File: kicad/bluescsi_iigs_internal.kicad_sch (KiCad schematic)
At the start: 27 parts, among them J1 Conn_02x13_Odd_Even, J2 Conn_02x13_Odd_Even, J3 105162-0001, J4 Conn_01x02_Male, J5 Conn_01x02_Male, J6 DB25_Male, M1 Screw_Terminal_01x01, M2 Screw_Terminal_01x01, SW1 SW_SPDT, U1 YAAJ_BluePill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

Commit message: added part numbers
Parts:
- C1, C2: value 4.7uF, 6.3v -> (none); footprint Capacitor_Tantalum_SMD:CP_EIA-3528-21_Kemet-B_Pad1.50x2.35mm_HandSolder -> (none); DESCRIPTION (none) -> 2.2uF 6.3V CASE-B_3528 Tantalum Capacitor; LCSC part number (none) -> C19276; MANUFACTURER_NAME (none) -> Kyocera AVX; MANUFACTURER_PART_NUMBER (none) -> TAJB225K035RNJ
- C3: value 4.7uF, 6.3v -> (none); footprint Capacitor_Tantalum_SMD:CP_EIA-3528-21_Kemet-B_Pad1.50x2.35mm_HandSolder -> (none); DESCRIPTION (none) -> 4.7uF 6.3V CASE-B_3528 Tantalum Capacitor; LCSC part number (none) -> C7204; MANUFACTURER_NAME (none) -> Kyocera AVX; MANUFACTURER_PART_NUMBER (none) -> TAJB475K016RNJ
- C4: value 1uF -> (none); footprint Capacitor_Tantalum_SMD:CP_EIA-3528-21_Kemet-B_Pad1.50x2.35mm_HandSolder -> (none); DESCRIPTION (none) -> 1uF 6.3V CASE-B_3528 Tantalum Capacitor; LCSC part number (none) -> C7192; MANUFACTURER_NAME (none) -> Kyocera AVX; MANUFACTURER_PART_NUMBER (none) -> TAJB105K035RNJ
- C5: value 0.1uF -> (none); footprint Capacitor_Tantalum_SMD:CP_EIA-3528-21_Kemet-B_Pad1.50x2.35mm_HandSolder -> (none); DESCRIPTION (none) -> 100nF 35V CASE-A_3216 Tantalum Capacitor; LCSC part number (none) -> C122257; MANUFACTURER_NAME (none) -> KEMET; MANUFACTURER_PART_NUMBER (none) -> T491A104K035AT
- D1: value LED -> (none); footprint LED_SMD:LED_0805_2012Metric_Pad1.15x1.40mm_HandSolder -> (none); DESCRIPTION (none) -> 0805 Blue LED; LCSC part number (none) -> C497961; MANUFACTURER_NAME (none) -> HONGLITRONIC(Hongli Zhihui (HONGLITRONIC)); MANUFACTURER_PART_NUMBER (none) -> HL-PSC-2012H203BC
- D2: value LED -> (none); footprint LED_SMD:LED_0805_2012Metric_Pad1.15x1.40mm_HandSolder -> (none); DESCRIPTION (none) -> 0805 Red LED; LCSC part number (none) -> C84256; MANUFACTURER_NAME (none) -> Foshan NationStar Optoelectronics; MANUFACTURER_PART_NUMBER (none) -> NCD0805R1
- D3: value Zener 5.6v -> (none); footprint Diode_SMD:D_SOD-123 -> (none); DESCRIPTION (none) -> 5.6V SOD-123 Zener Diode; LCSC part number (none) -> C268592; MANUFACTURER_NAME (none) -> PANJIT International; MANUFACTURER_PART_NUMBER (none) -> MMSZ5232A_R1_00001
- F1: value Fuse -> (none); footprint Fuse:Fuse_1210_3225Metric -> (none); DESCRIPTION (none) -> SMD 1206 Fuse 800mA 63V; LCSC part number (none) -> C163134; MANUFACTURER_NAME (none) -> TA-I Tech; MANUFACTURER_PART_NUMBER (none) -> CFS12V6TR80
- J1, J2: value Conn_02x13_Odd_Even -> (none); footprint Connector_PinHeader_2.54mm:PinHeader_2x13_P2.54mm_Vertical -> (none)
- J3: value 105162-0001 -> (none); footprint Molex 105162-0001:105162-0001 -> (none); LCSC part number (none) -> C724031
- J4, J5: value Conn_01x02_Male -> (none); footprint Connector_PinHeader_2.54mm:PinHeader_1x02_P2.54mm_Vertical -> (none)
- J6: value DB25_Male -> (none); footprint Connector_Dsub:DSUB-25_Male_EdgeMount_P2.77mm -> (none)
- JP1, JP2: value Jumper_3_Open -> (none); footprint Jumper:SolderJumper-3_P1.3mm_Open_Pad1.0x1.5mm_NumberLabels -> (none)
- M1, M2: value Screw_Terminal_01x01 -> (none); footprint my library:keystone-7774 -> (none)
- R1: value 110 -> (none); footprint Resistor_SMD:R_0805_2012Metric_Pad1.20x1.40mm_HandSolder -> (none); DESCRIPTION (none) -> 100Ω 0805 Chip Resistor - Surface Mount; LCSC part number (none) -> C17408; MANUFACTURER_NAME (none) -> UNI-ROYAL(Uniroyal Elec); MANUFACTURER_PART_NUMBER (none) -> 0805W8F1000T5E
- R2: value 1K -> (none); footprint Resistor_SMD:R_0805_2012Metric_Pad1.20x1.40mm_HandSolder -> (none); DESCRIPTION (none) -> 1KΩ 0805 Chip Resistor - Surface Mount; LCSC part number (none) -> C17513; MANUFACTURER_NAME (none) -> UNI-ROYAL(Uniroyal Elec); MANUFACTURER_PART_NUMBER (none) -> 0805W8F1001T5E
- SW1: value SW_SPDT -> (none); footprint Button_Switch_SMD:SW_SPDT_PCM12 -> (none); DESCRIPTION (none) -> SMD Slide Switch; LCSC part number (none) -> C221841; MANUFACTURER_NAME (none) -> C&K; MANUFACTURER_PART_NUMBER (none) -> PCM12SMTR
- U1: value YAAJ_BluePill -> (none); footprint my library:YAAJ_BluePill_2 -> (none)
- U2, U3: value UC560x, UCC56xx -> (none); footprint my library:SOIC127P600X175-16N -> (none)
- U4: value UCC3916 -> (none); footprint Package_SO:SOIC-8_3.9x4.9mm_P1.27mm -> (none)
- U5: value NL17SZ07DFT2G -> (none); footprint Package_TO_SOT_SMD:SOT-353_SC-70-5_Handsoldering -> (none); DESCRIPTION (none) -> Open Drain 24mA Buffers，Unidirectional Voltage Level Transl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; LCSC part number (none) -> C113255; MANUFACTURER_NAME (none) -> onsemi; MANUFACTURER_PART_NUMBER (none) -> NL17SZ07DFT2G

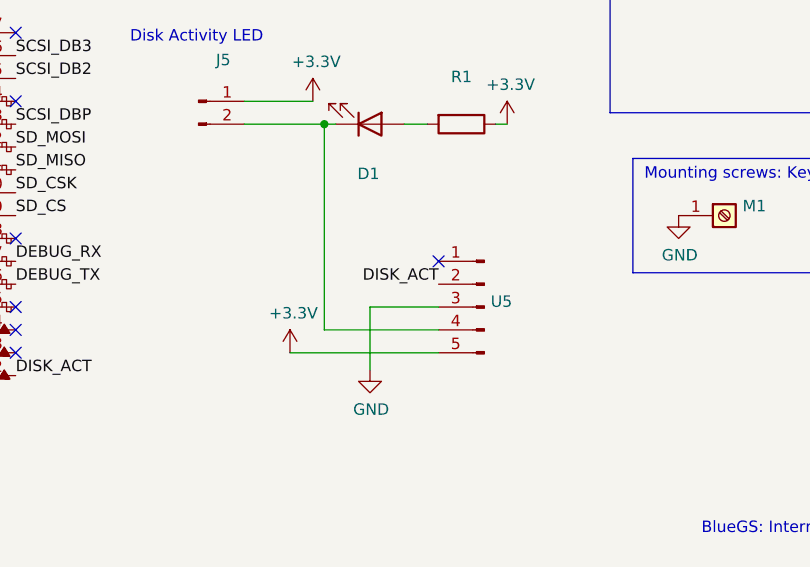
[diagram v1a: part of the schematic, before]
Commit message: Added compatibility for 74LVC1G125SE in place of NL17SZ07DFT2G
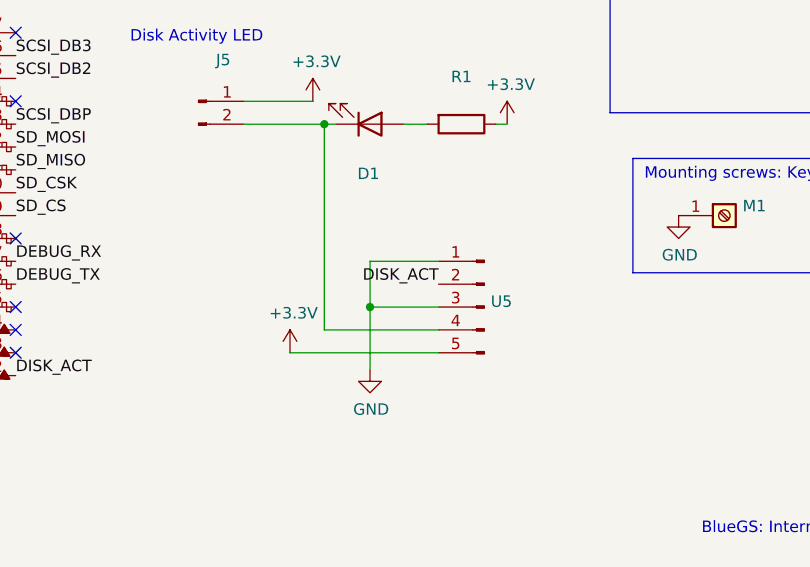
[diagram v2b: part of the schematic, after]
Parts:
- C1, C2: LCSC part number C19276 -> C444753; MANUFACTURER_PART_NUMBER TAJB225K035RNJ -> TAJB225M020RNJ
- C3: LCSC part number C7204 -> C918865; MANUFACTURER_NAME Kyocera AVX -> KEMET; MANUFACTURER_PART_NUMBER TAJB475K016RNJ -> T494B475K016AT
- C4: LCSC part number C7192 -> C452761; MANUFACTURER_NAME Kyocera AVX -> KEMET; MANUFACTURER_PART_NUMBER TAJB105K035RNJ -> T491B105K025AT
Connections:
- net GND: now also U5.1 (Pin_1)
- no-connect marks 14 -> 13
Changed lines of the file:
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@@
   (junction (at 167.64 114.3) (diameter 0) (color 0 0 0 0)
+  )
+  (junction (at 149.86 165.1) (diameter 0) (color 0 0 0 0)
   )
   (junction (at 167.64 116.84) (diameter 0) (color 0 0 0 0)
@@
   (no_connect (at 110.49 134.62))
   (no_connect (at 69.85 152.4))
-  (no_connect (at 157.48 160.02))
   (no_connect (at 167.64 106.68))
   (no_connect (at 110.49 167.64))
@@
     (stroke (width 0) (type default) (color 0 0 0 0))
   )
+  (wire (pts (xy 149.86 160.02) (xy 149.86 165.1))
+    (stroke (width 0) (type default) (color 0 0 0 0))
+  )
   (wire (pts (xy 144.78 144.78) (xy 146.05 144.78))
     (stroke (width 0) (type default) (color 0 0 0 0))
@@
   )
   (wire (pts (xy 214.63 116.205) (xy 216.535 116.205))
+    (stroke (width 0) (type default) (color 0 0 0 0))
+  )
+  (wire (pts (xy 157.48 160.02) (xy 149.86 160.02))
     (stroke (width 0) (type default) (color 0 0 0 0))
   )
@@
       (effects (font (size 1.27 1.27)) hide)
     )
-    (property "MANUFACTURER_NAME" "Kyocera AVX" (id 4) (at 261.62 38.1 0)
-      (effects (font (size 1.27 1.27)) hide)
-    )
-    (property "MANUFACTURER_PART_NUMBER" "TAJB475K016RNJ" (id 5) (at 261.62 38.1 0)
+    (property "MANUFACTURER_NAME" "KEMET" (id 4) (at 261.62 38.1 0)
+      (effects (font (size 1.27 1.27)) hide)
+    )
+    (property "MANUFACTURER_PART_NUMBER" "T494B475K016AT" (id 5) (at 261.62 38.1 0)
       (effects (font (size 1.27 1.27)) hide)
     )
@@
       (effects (font (size 1.27 1.27)) hide)
     )
-    (property "LCSC part number" "C7204" (id 7) (at 261.62 38.1 0)
+    (property "LCSC part number" "C918865" (id 7) (at 261.62 38.1 0)
       (effects (font (size 1.27 1.27)) hide)
     )
@@
       (effects (font (size 1.27 1.27)) hide)
     )
-    (property "MANUFACTURER_PART_NUMBER" "TAJB225K035RNJ" (id 5) (at 130.81 39.37 0)
+    (property "MANUFACTURER_PART_NUMBER" "TAJB225M020RNJ" (id 5) (at 130.81 39.37 0)
       (effects (font (size 1.27 1.27)) hide)
     )
@@
       (effects (font (size 1.27 1.27)) hide)
     )
-    (property "LCSC part number" "C19276" (id 7) (at 130.81 39.37 0)
+    (property "LCSC part number" "C444753" (id 7) (at 130.81 39.37 0)
       (effects (font (size 1.27 1.27)) hide)
     )
@@
       (effects (font (size 1.27 1.27)) hide)
     )
-    (property "MANUFACTURER_PART_NUMBER" "TAJB225K035RNJ" (id 5) (at 130.81 67.31 0)
+    (property "MANUFACTURER_PART_NUMBER" "TAJB225M020RNJ" (id 5) (at 130.81 67.31 0)
       (effects (font (size 1.27 1.27)) hide)
     )
@@
       (effects (font (size 1.27 1.27)) hide)
     )
-    (property "LCSC part number" "C19276" (id 7) (at 130.81 67.31 0)
+    (property "LCSC part number" "C444753" (id 7) (at 130.81 67.31 0)
       (effects (font (size 1.27 1.27)) hide)
     )
@@
       (effects (font (size 1.27 1.27)) hide)
     )
-    (property "MANUFACTURER_NAME" "Kyocera AVX" (id 4) (at 232.41 120.015 0)
-      (effects (font (size 1.27 1.27)) hide)
-    )
-    (property "MANUFACTURER_PART_NUMBER" "TAJB105K035RNJ" (id 5) (at 232.41 120.015 0)
+    (property "MANUFACTURER_NAME" "KEMET" (id 4) (at 232.41 120.015 0)
+      (effects (font (size 1.27 1.27)) hide)
+    )
+    (property "MANUFACTURER_PART_NUMBER" "T491B105K025AT" (id 5) (at 232.41 120.015 0)
       (effects (font (size 1.27 1.27)) hide)
     )
@@
       (effects (font (size 1.27 1.27)) hide)
     )
-    (property "LCSC part number" "C7192" (id 7) (at 232.41 120.015 0)
-      (effects (font (size 1.27 1.27)) hide)
-    )
+    (property "LCSC part number" "C452761" (id 7) (at 232.41 120.015 0)
+      (effects (font (size 1.27 1.27)) hide)
+    )

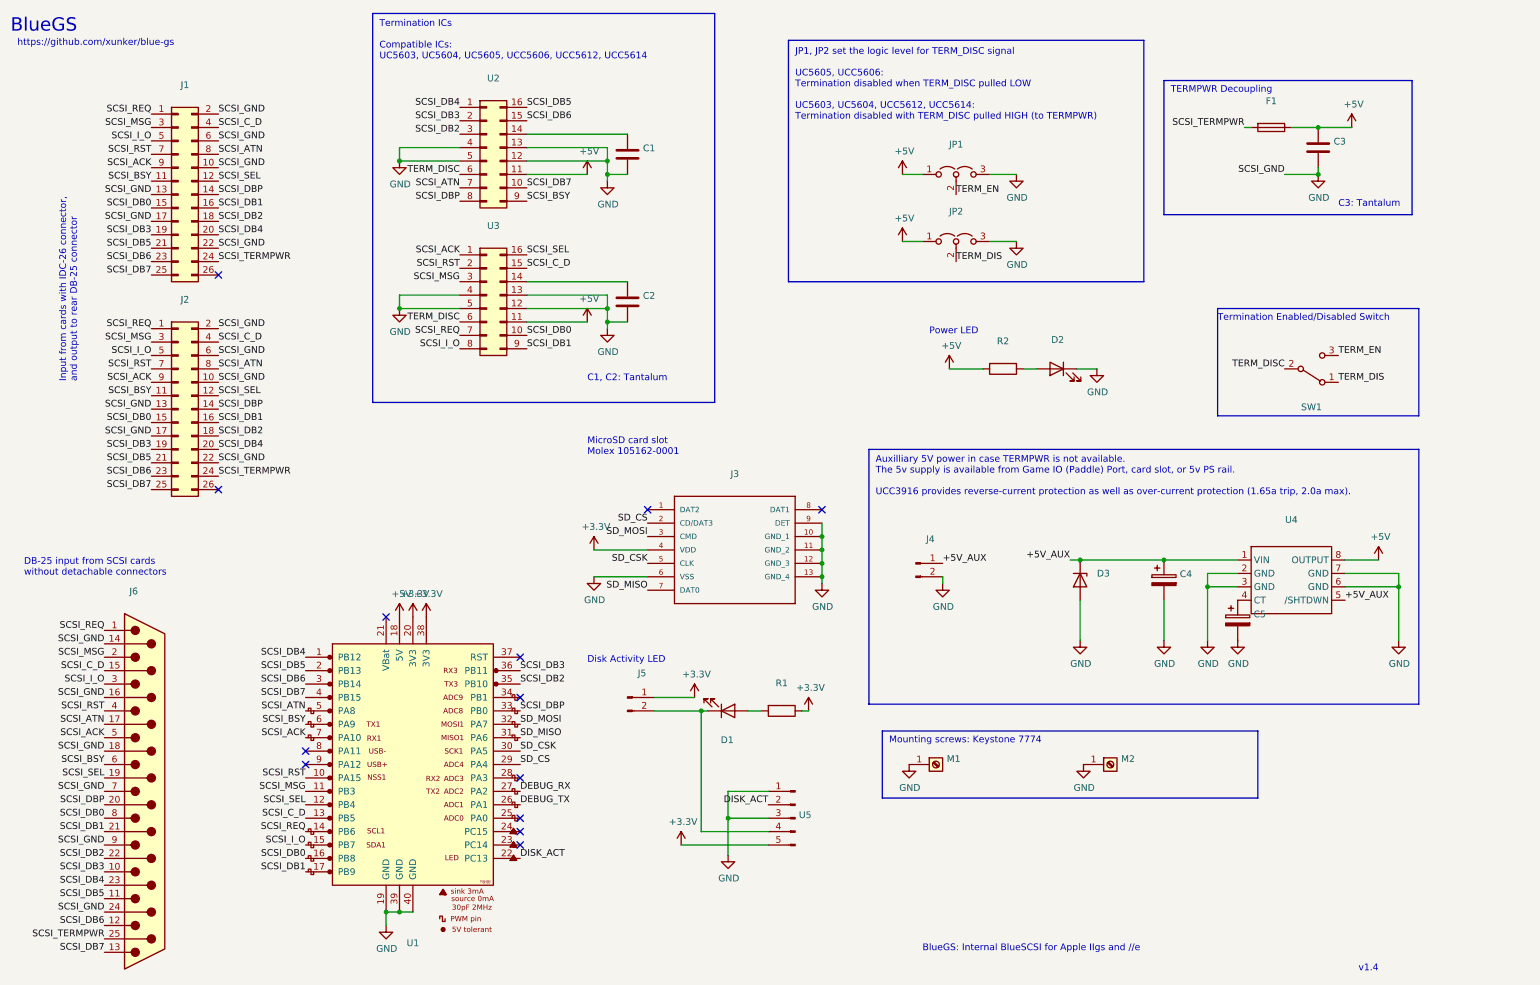
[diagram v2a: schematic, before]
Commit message: Add silkscreen notes about connections
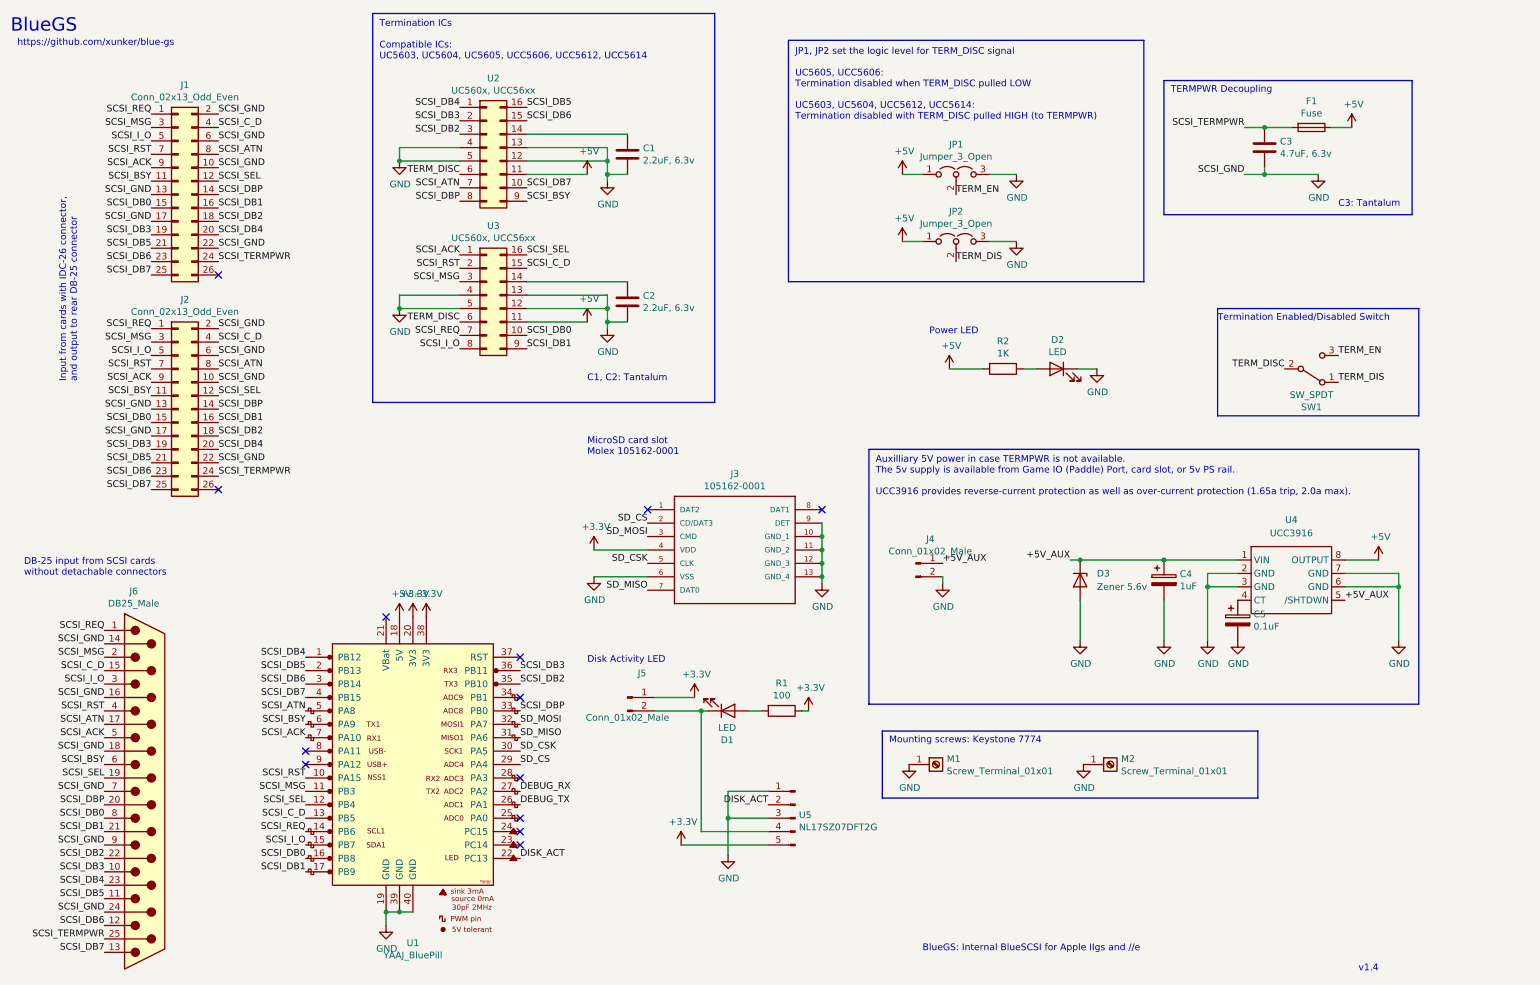
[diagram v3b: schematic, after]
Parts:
- C1, C2: value (none) -> 2.2uF, 6.3v; footprint (none) -> Capacitor_Tantalum_SMD:CP_EIA-3528-21_Kemet-B_Pad1.50x2.35mm_HandSolder
- C3: value (none) -> 4.7uF, 6.3v; footprint (none) -> Capacitor_Tantalum_SMD:CP_EIA-3528-21_Kemet-B_Pad1.50x2.35mm_HandSolder
- C4: value (none) -> 1uF; footprint (none) -> Capacitor_Tantalum_SMD:CP_EIA-3528-21_Kemet-B_Pad1.50x2.35mm_HandSolder
- C5: value (none) -> 0.1uF; footprint (none) -> Capacitor_Tantalum_SMD:CP_EIA-3216-10_Kemet-I
- D1, D2: value (none) -> LED; footprint (none) -> LED_SMD:LED_0805_2012Metric_Pad1.15x1.40mm_HandSolder
- D3: value (none) -> Zener 5.6v; footprint (none) -> Diode_SMD:D_SOD-123
- F1: value (none) -> Fuse; footprint (none) -> Fuse:Fuse_1210_3225Metric
- J1, J2: value (none) -> Conn_02x13_Odd_Even; footprint (none) -> Connector_PinHeader_2.54mm:PinHeader_2x13_P2.54mm_Vertical
- J3: value (none) -> 105162-0001; footprint (none) -> Molex 105162-0001:105162-0001
- J4, J5: value (none) -> Conn_01x02_Male; footprint (none) -> Connector_PinHeader_2.54mm:PinHeader_1x02_P2.54mm_Vertical
- J6: value (none) -> DB25_Male; footprint (none) -> Connector_Dsub:DSUB-25_Male_EdgeMount_P2.77mm
- JP1, JP2: value (none) -> Jumper_3_Open; footprint (none) -> Jumper:SolderJumper-3_P1.3mm_Open_Pad1.0x1.5mm_NumberLabels
- M1, M2: value (none) -> Screw_Terminal_01x01; footprint (none) -> my library:keystone-7774
- R1: value (none) -> 100; footprint (none) -> Resistor_SMD:R_0805_2012Metric_Pad1.20x1.40mm_HandSolder
- R2: value (none) -> 1K; footprint (none) -> Resistor_SMD:R_0805_2012Metric_Pad1.20x1.40mm_HandSolder
- SW1: value (none) -> SW_SPDT; footprint (none) -> Button_Switch_SMD:SW_SPDT_PCM12
- U1: value (none) -> YAAJ_BluePill; footprint (none) -> my library:YAAJ_BluePill_2
- U2, U3: value (none) -> UC560x, UCC56xx; footprint (none) -> my library:SOIC127P600X175-16N
- U4: value (none) -> UCC3916; footprint (none) -> Package_SO:SOIC-8_3.9x4.9mm_P1.27mm
- U5: value (none) -> NL17SZ07DFT2G; footprint (none) -> Package_TO_SOT_SMD:SOT-353_SC-70-5_Handsoldering
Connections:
- net +5V: no longer C3.1
- net SCSI_TERMPWR: now also C3.1
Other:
- moved on the sheet: C3, F1

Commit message: Change board branding to "BlueGS / BP" to distinguish it from rp2040-based design. Move cd card slot back slightly.
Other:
- note added: "12/2022"
- note added: "5v is available from the Game IO (Paddle) socket, a card slot, the 5V PS rail, or an external supply. Apple II_{GS} users can also use the fan connector in conjunction with a 12V-to-5V regulator."
- note added: "Auxilliary 5V power in case TERMPWR is not available."
- note added: "Blue-Pill-based Internal BlueSCSI for Apple II_{GS} and //e"
- note added: "BlueGS / BP"
- note added: "C1, C2: Tantalum, 6.3v minimum. Use highest rating you can find for the package size."
- note added: "C3: Tantalum, 6.3v minimum. Use highest voltage rating you can find for the package. Capacitor should be placed as close to SCSI connectors as possible."
- note added: "CC BY-SA-NC/4.0"
- note added: "NEVER CONNECT PIN 1 TO PIN 3 UNDER ANY CIRCUMSTANCES"
- note added: "UCC3916 provides reverse-current protection as well as over-current protection (1.65A trip, 2.0A max)."
- note added: "You can bypass this section by soldering a 1N5817 Schottky Diode (SOD-123 package) from pin 1 (anode side) to pin 8 (cathode side) of pad for UCC3916. The diode will provide reverse-current protection but has a larger voltage drop and has no over-current protection."
- note removed: "Auxilliary 5V power in case TERMPWR is not available. The 5v supply is available from Game IO (Paddle) Port, card slot, or 5v PS rail. UCC3916 provides reverse-current protection as well as over-current protection (1.65a trip, 2.0a max)."
- note removed: "C1, C2: Tantalum"
- note removed: "C3: Tantalum"
- moved on the sheet: C4, C5, D1, D3, J4, J5, JP1, JP2, R1, U1, U4, U5
